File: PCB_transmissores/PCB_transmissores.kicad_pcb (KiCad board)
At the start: 2 copper layers, 109.2 x 63.5 mm, 7 parts, among them J1 Screw_Terminal_01x02

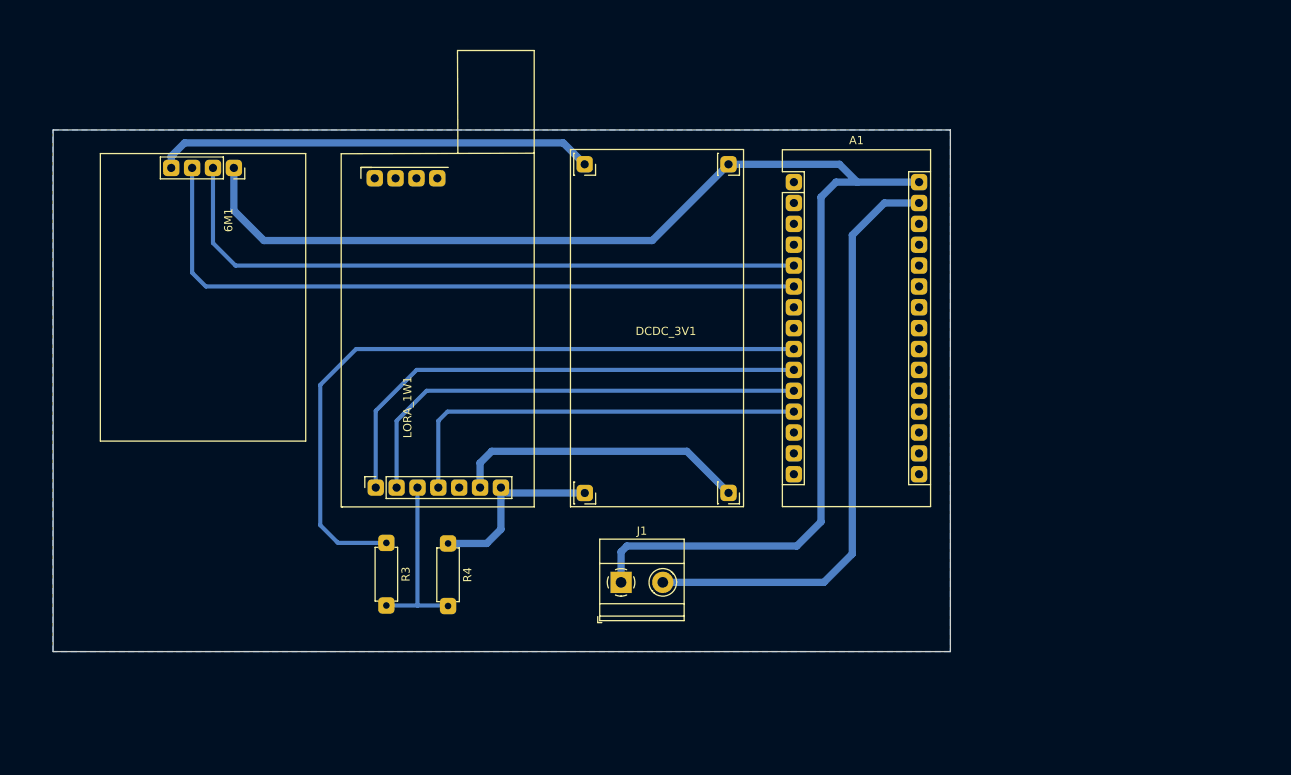
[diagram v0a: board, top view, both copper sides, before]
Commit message: Modificações placa transmissores
Adicionado:
Suporte de bateria
Furos de fixação
Resistores divisores de tensão
Corrigida a posição dos pinos do módulo GPS
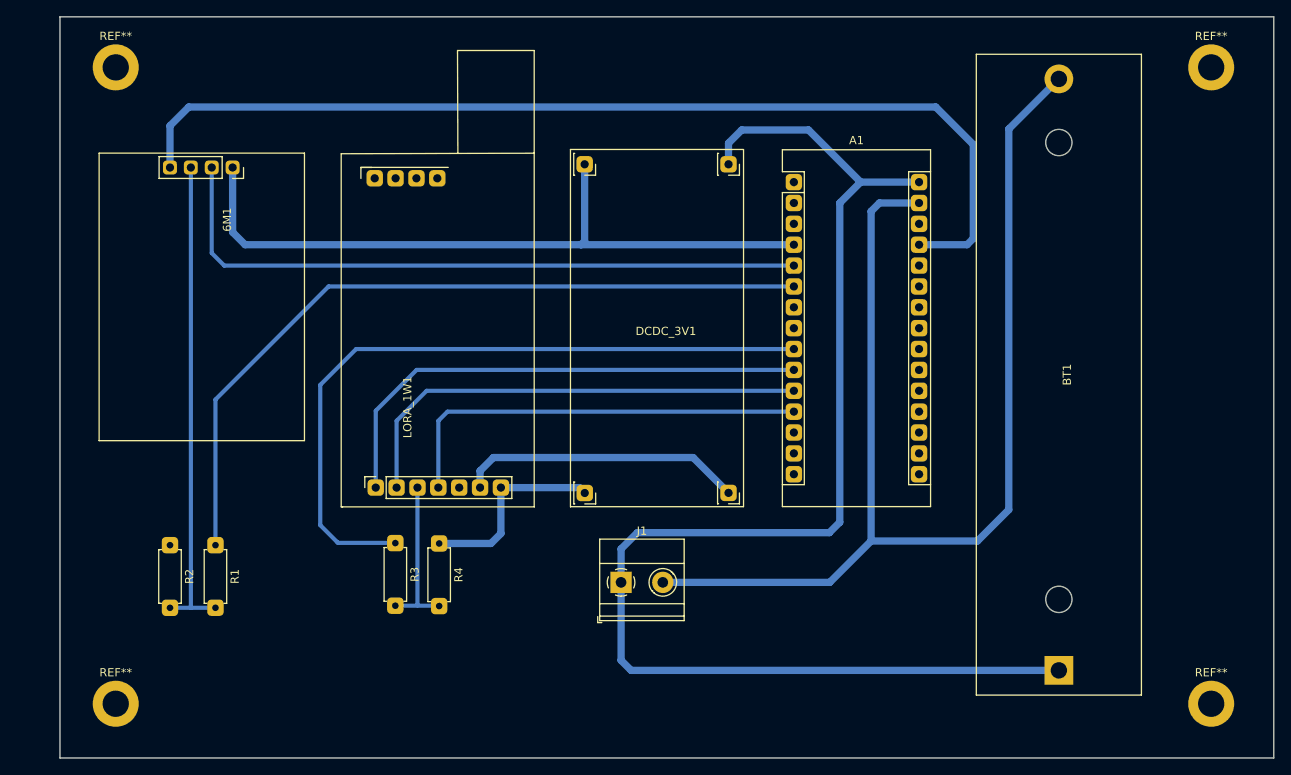
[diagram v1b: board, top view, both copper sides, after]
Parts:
- added BT1: Battery_Cell, Battery:BatteryHolder_MPD_BH-18650-PC2, F.Cu at (211.3, 139.4)
- added R1: 1k, Resistor_THT:R_Axial_DIN0207_L6.3mm_D2.5mm_P7.62mm_Horizontal, F.Cu at (108.7, 124.2)
- added R2: 0,5k, Resistor_THT:R_Axial_DIN0207_L6.3mm_D2.5mm_P7.62mm_Horizontal, F.Cu at (103.1, 124.2)
- added REF**: MountingHole_3.2mm_M3_DIN965_Pad, MountingHole:MountingHole_3.2mm_M3_DIN965_Pad, F.Cu at (229.9, 66.0)
- added REF**: MountingHole_3.2mm_M3_DIN965_Pad, MountingHole:MountingHole_3.2mm_M3_DIN965_Pad, F.Cu at (229.9, 143.5)
- added REF**: MountingHole_3.2mm_M3_DIN965_Pad, MountingHole:MountingHole_3.2mm_M3_DIN965_Pad, F.Cu at (96.5, 66.0)
- added REF**: MountingHole_3.2mm_M3_DIN965_Pad, MountingHole:MountingHole_3.2mm_M3_DIN965_Pad, F.Cu at (96.5, 143.5)
- moved R3 1.09 mm to (130.6, 124.0)
- moved R4 1.08 mm to (135.9, 124.0)
- moved 6M1 0.16 mm to (110.7, 78.2)
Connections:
- 6M1 pad 4: VIN -> 5V_NANO
- A1 pad 5: RX_GPS -> TX_GPS
- A1 pad 6: TX_GPS -> Net-(A1-Pad6)
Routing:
- net 5V_NANO: track 0.00 -> 124.1 mm
- net GND: track 150.8 -> 259.9 mm
- net Net-(A1-Pad6): track 0.00 -> 93.8 mm
- net RX_GPS: track 81.0 -> 59.1 mm
- net TX_GPS: track 86.7 -> 82.9 mm
- net VIN: track 169.1 -> 166.8 mm
- net RX_LORA: track 21.9 -> 19.7 mm
- net 3.3V_DCDC: track 35.9 -> 34.7 mm
- removed copper zone on B.Cu, net GND
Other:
- board size 109.2 x 63.5 mm -> 147.8 x 90.2 mm

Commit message: Subtituito StepDown por StepUp
Substituido o uso do StepDown DcDc por StepUp DcDc.
Feitas modificações em trilhas e ligações para adaptar o circuito a mudança.
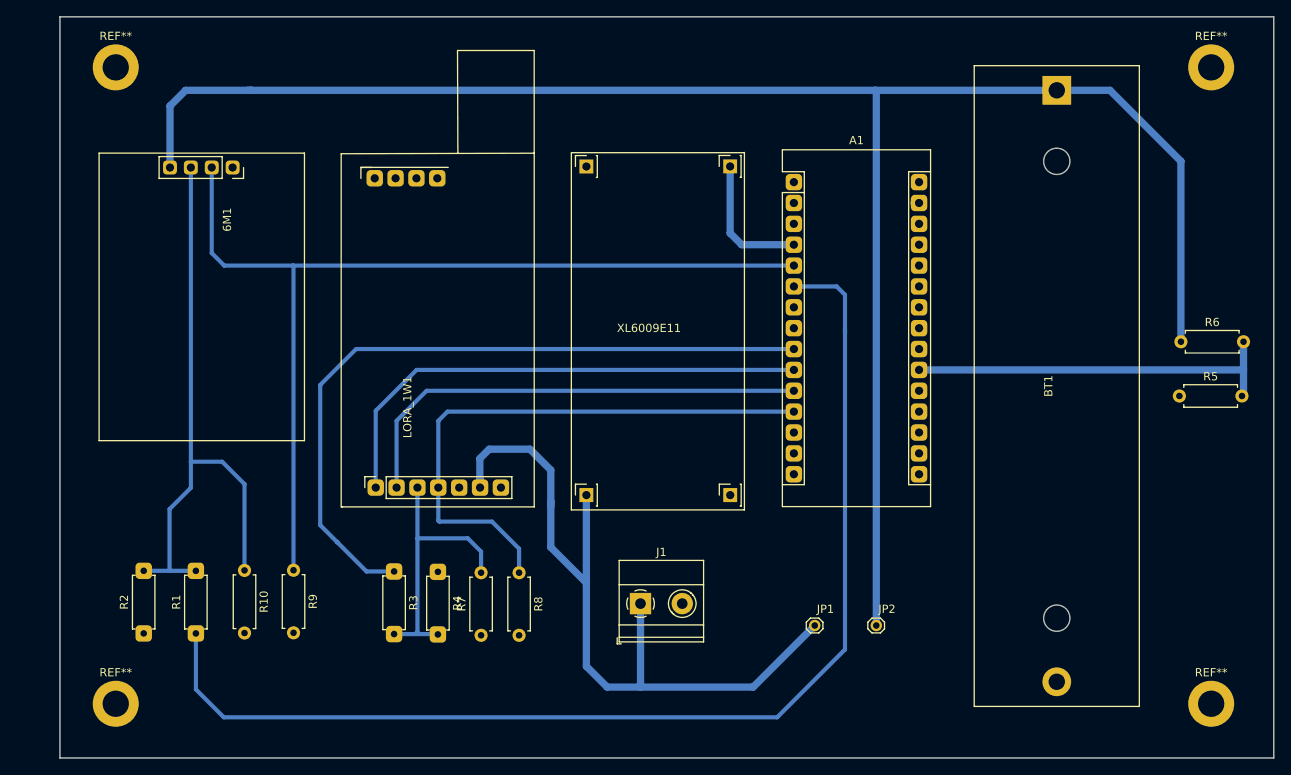
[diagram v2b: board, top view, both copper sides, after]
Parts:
- removed DCDC_3V1: DCDC_CHINA, Converter_DCDC:STEPDOWN_CHINA
- added JP1: Jumper, TestPoint:Furo_Jumper, F.Cu at (181.6, 134.0)
- added JP2: Jumper, TestPoint:Furo_Jumper, F.Cu at (189.1, 134.0)
- added R10: 4k7, Resistor_THT:R_Axial_DIN0207_L6.3mm_D2.5mm_P7.62mm_Horizontal, F.Cu at (112.2, 127.3)
- added R5: 500k, Resistor_THT:R_Axial_DIN0207_L6.3mm_D2.5mm_P7.62mm_Horizontal, F.Cu at (226.0, 106.0)
- added R6: 5000k, Resistor_THT:R_Axial_DIN0207_L6.3mm_D2.5mm_P7.62mm_Horizontal, F.Cu at (226.2, 99.4)
- added R7: 4k7, Resistor_THT:R_Axial_DIN0207_L6.3mm_D2.5mm_P7.62mm_Horizontal, F.Cu at (141.0, 135.2)
- added R8: 4k7, Resistor_THT:R_Axial_DIN0207_L6.3mm_D2.5mm_P7.62mm_Horizontal, F.Cu at (145.6, 127.6)
- added R9: 4k7, Resistor_THT:R_Axial_DIN0207_L6.3mm_D2.5mm_P7.62mm_Horizontal, F.Cu at (118.2, 127.3)
- added XL6009E11: STEPUP, Converter_DCDC:STEPUP_XL6009E1, F.Cu at (171.3, 118.1)
- moved BT1 70.6 mm to (211.1, 68.8), turned to 270 degrees
- moved R2 11.2 mm to (99.9, 134.9), turned to 90 degrees
- moved R1 11.0 mm to (106.3, 134.9), turned to 90 degrees
- moved J1 3.51 mm to (160.4, 131.3)
- moved R3 3.46 mm to (130.4, 127.4)
- moved R4 3.46 mm to (135.7, 127.5)
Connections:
- net Net-(A1-Pad6) renamed D3
- net Net-(A1-Pad9) renamed D6
- net TX_GPS renamed D2
- net TX_LORA renamed D9
- 6M1 pad 4: 5V_NANO -> VIN
- A1 pad 21: Net-(A1-Pad21) -> A2
- A1 pad 27: 5V_NANO -> Net-(A1-Pad27)
- A1 pad 30: VIN -> 7V_STEPUP
- LORA_1W1 pad 6: 3.3V_DCDC -> VIN
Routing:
- net GND: track 259.9 -> 18.4 mm
- net VIN: track 166.8 -> 315.4 mm
- net 5V_NANO: track 124.1 -> 0.00 mm
- net D3: track 93.8 -> 143.0 mm
- net A2: track 0.00 -> 46.2 mm
- net D2: track 82.9 -> 120.0 mm
- net 3.3V_DCDC: track 34.7 -> 0.00 mm
- net D9: track 51.9 -> 70.1 mm
- net RX_GPS: track 59.1 -> 74.7 mm
- net RX_LORA: track 19.7 -> 34.3 mm
- net D6: track 85.5 -> 88.0 mm

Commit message: atualização da placa dos transmissores
Up
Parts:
- removed BT1: Battery_Cell, Battery:BatteryHolder_MPD_BH-18650-PC2
- removed J1: Screw_Terminal_01x02, TerminalBlock_Phoenix:TerminalBlock_Phoenix_MKDS-1,5-2-5.08_1x02_P5.08mm_Horizontal
- removed JP1, JP2: Jumper, TestPoint:Furo_Jumper
- removed LORA_1W1: LORA_433T30D, RF_WiFi:LORA_E32_433T30D
- removed REF** (x4): MountingHole_3.2mm_M3_DIN965_Pad, MountingHole:MountingHole_3.2mm_M3_DIN965_Pad
- removed XL6009E11: STEPUP, Converter_DCDC:STEPUP_XL6009E1
- added H1: MountingHole, MountingHole:MountingHole_5.5mm, F.Cu at (91.2, 104.4)
- added H2: MountingHole, MountingHole:MountingHole_5.5mm, F.Cu at (138.4, 74.7)
- added J2: Barrel_Jack_MountingPin, Connector_BarrelJack:BarrelJack_Wuerth_6941xx301002, F.Cu at (182.6, 70.9)
- added LORA_100mW1: LORA_433T20D, RF_WiFi:LORA_E32_433T20D, F.Cu at (104.1, 119.1)
- added XL40051: STEPDOWN, Converter_DCDC:STEPDOWN_XL4005, F.Cu at (154.4, 83.1)
- R5: value 500k -> 5k
- R6: value 5000k -> 36k
- moved 6M1 46.8 mm to (133.6, 119.1), turned to 90 degrees
- moved R2 44.1 mm to (144.0, 134.1)
- moved R1 41.6 mm to (147.8, 134.1)
- moved R7 36.8 mm to (104.6, 140.7)
- moved R5 29.7 mm to (199.1, 118.6), turned to 90 degrees
- moved R4 29.6 mm to (109.2, 140.7), turned to 90 degrees
- moved R10 28.0 mm to (140.2, 126.5)
- moved R6 27.1 mm to (199.1, 97.8), turned to 270 degrees
- moved R8 25.0 mm to (120.7, 128.5)
- moved R3 21.5 mm to (113.5, 140.7), turned to 90 degrees
- moved R9 13.7 mm to (131.8, 126.2)
- moved A1 4.93 mm to (178.1, 84.8)
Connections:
- 6M1 pad 2: D2 -> D11
- 6M1 pad 4: VIN -> 3,3v
- A1 pad 14: Net-(A1-Pad14) -> D11
- A1 pad 15: Net-(A1-Pad15) -> D12
- A1 pad 30: 7V_STEPUP -> VIN
- A1 pad 5: D2 -> Net-(A1-Pad5)
- A1 pad 6: D3 -> Net-(A1-Pad6)
- R1 pad 1: D3 -> D12
- R9 pad 1: D2 -> D11
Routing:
- net VIN: track 315.4 -> 60.2 mm
- net D3: track 143.0 -> 0.00 mm
- net D2: track 120.0 -> 0.00 mm
- net D11: track 0.00 -> 88.1 mm
- net 3,3v: track 0.00 -> 70.6 mm
- net RX_GPS: track 74.7 -> 23.2 mm
- net D12: track 0.00 -> 41.3 mm
- net A2: track 46.2 -> 11.4 mm
- net D6: track 88.0 -> 111.7 mm
- net M0: track 62.3 -> 84.9 mm
- net M1: track 58.0 -> 78.5 mm
- net D9: track 70.1 -> 88.8 mm
- net GND: track 18.4 -> 0.00 mm
- net RX_LORA: track 34.3 -> 28.3 mm
- added copper zone on B.Cu, net GND
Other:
- board size 147.8 x 90.2 mm -> 120.1 x 80 mm
